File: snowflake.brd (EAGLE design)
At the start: 68.6 x 68.6 mm, 28 parts, among them J1 M03X2-NOSILK

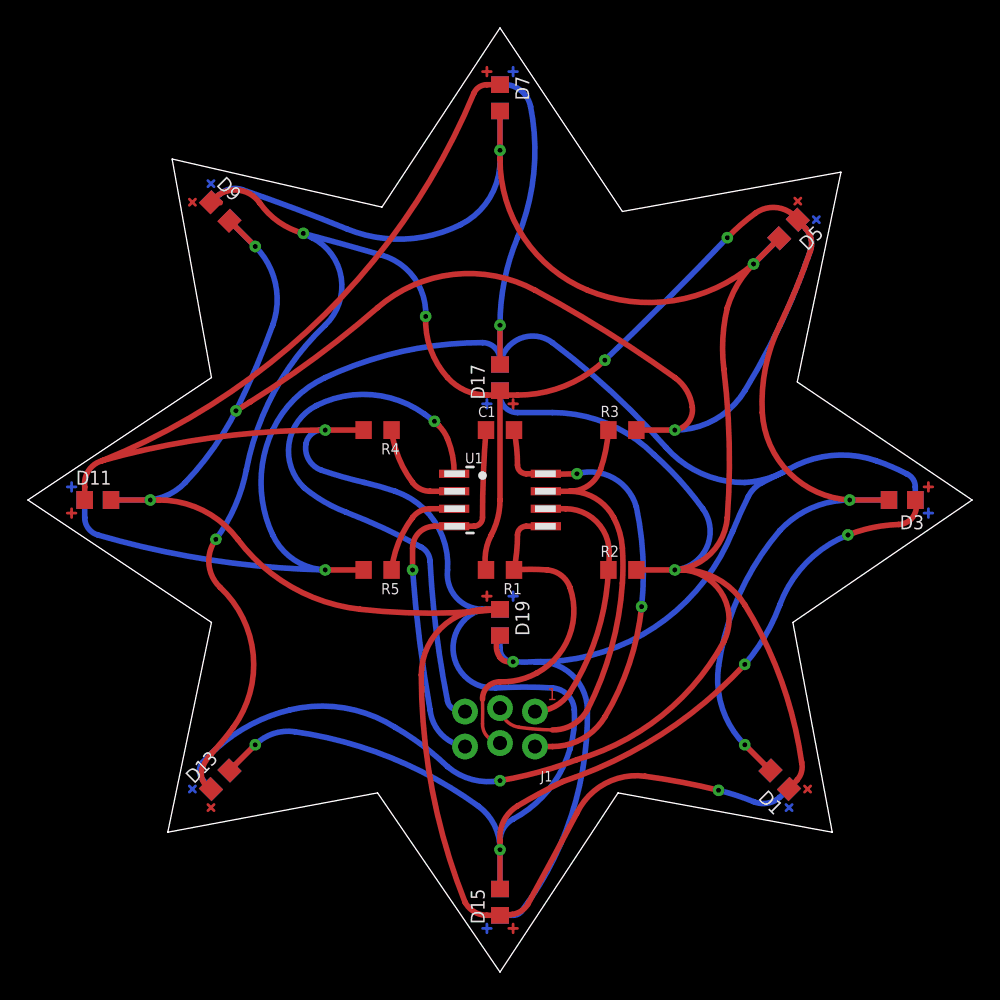
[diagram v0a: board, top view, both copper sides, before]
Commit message: Placed LED more logical.
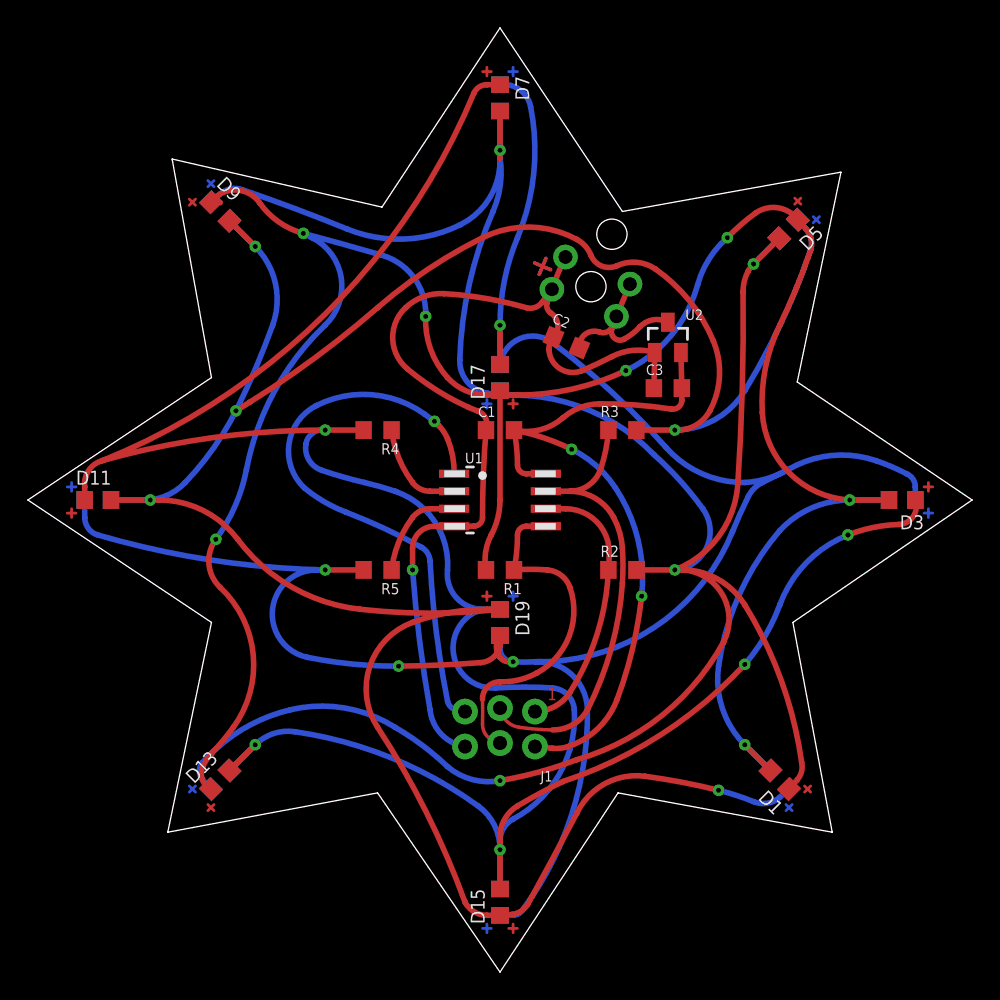
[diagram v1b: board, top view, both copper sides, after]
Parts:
- added C2, C3: (no value), snowflake:C0805NOSILK
- added J2: CON_TERMINAL_HOLES, adi-misc:TERMINAL_2P_4H
- added U2: V_REG_MCP170X-CB, adi-misc:SOT23
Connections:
- new net N$1: C2.2, J2.P$5, J2.P$6, U2.3
- net GND: now also C2.1, C3.1, J2.P$3, J2.P$4, U2.1
- net VCC: now also C3.2, U2.2
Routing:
- net GND: track 27.9 -> 69.3 mm
- net VCC: track 33.4 -> 52.9 mm
- net N$7: track 177.0 -> 190.2 mm
- net N$1: track 0.00 -> 11.8 mm
- net N$11: track 166.3 -> 157.3 mm, vias 3 -> 4
- net N$8: track 182.2 -> 176.9 mm
- net N$9: track 168.8 -> 169.6 mm
